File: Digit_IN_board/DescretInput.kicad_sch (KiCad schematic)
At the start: 21 parts, among them J4 DS1013-01-10RSiB-B (1), U5 HEF40106B (SO-14), U8 74LVC2G14

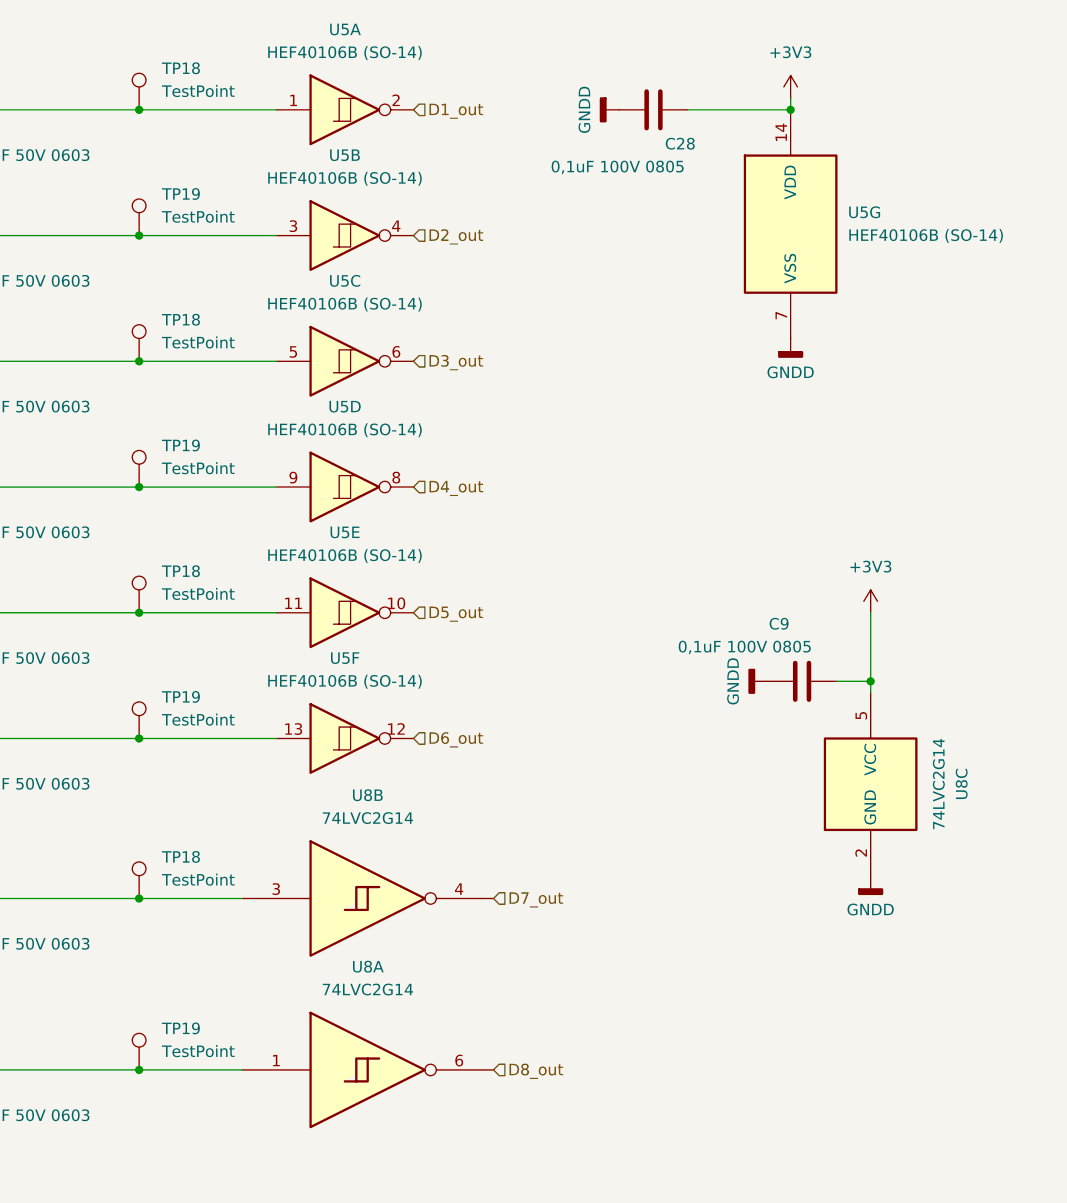
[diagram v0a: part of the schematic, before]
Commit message: Add DE USART 03.06.24
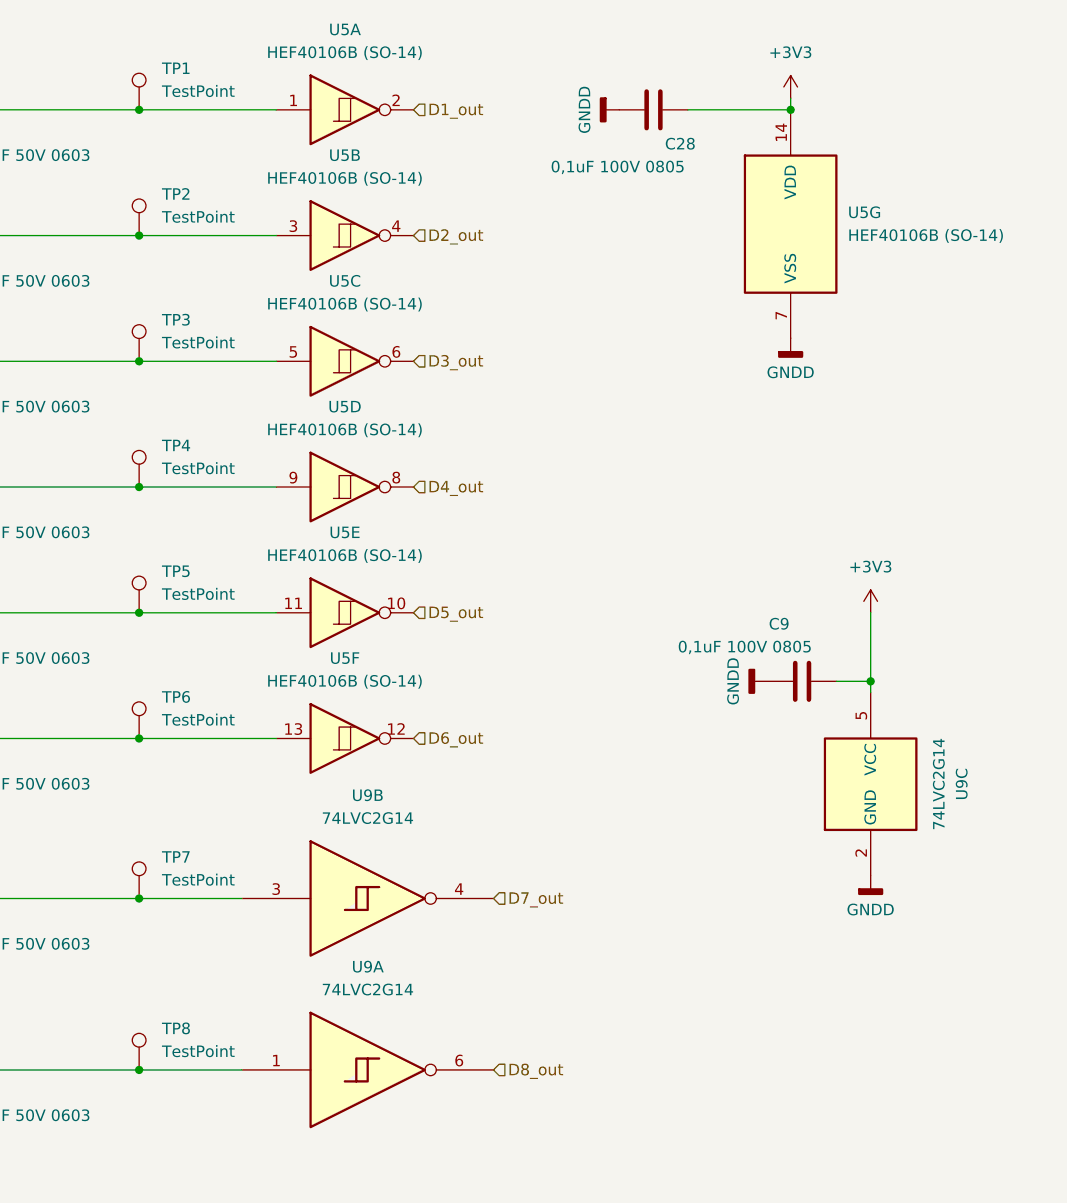
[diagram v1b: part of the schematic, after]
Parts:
- renumbered TP18 to TP1, TP19 to TP2, TP18 to TP3, TP19 to TP4, TP18 to TP5, TP19 to TP6, TP18 to TP7, TP19 to TP8, U8 to U9
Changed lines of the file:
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@@
   (symbol (lib_id "Connector:TestPoint") (at 185.42 100.33 0) (unit 1)
     (in_bom yes) (on_board yes) (dnp no) (fields_autoplaced)
-    (property "Reference" "TP19" (at 187.96 95.758 0)
+    (property "Reference" "TP6" (at 187.96 95.758 0)
       (effects (font (size 1.27 1.27)) (justify left))
     )
@@
   (symbol (lib_id "Connector:TestPoint") (at 185.42 58.42 0) (unit 1)
     (in_bom yes) (on_board yes) (dnp no)
-    (property "Reference" "TP18" (at 187.96 53.848 0)
+    (property "Reference" "TP3" (at 187.96 53.848 0)
       (effects (font (size 1.27 1.27)) (justify left))
     )
@@
   (symbol (lib_id "74xGxx:74LVC2G14") (at 266.7 105.41 0) (unit 3)
     (in_bom yes) (on_board yes) (dnp no) (fields_autoplaced)
-    (property "Reference" "U8" (at 276.86 105.41 90)
+    (property "Reference" "U9" (at 276.86 105.41 90)
       (effects (font (size 1.27 1.27)))
     )
@@
   (symbol (lib_id "Connector:TestPoint") (at 185.42 86.36 0) (unit 1)
     (in_bom yes) (on_board yes) (dnp no) (fields_autoplaced)
-    (property "Reference" "TP18" (at 187.96 81.788 0)
+    (property "Reference" "TP5" (at 187.96 81.788 0)
       (effects (font (size 1.27 1.27)) (justify left))
     )
@@
   (symbol (lib_id "74xGxx:74LVC2G14") (at 212.09 118.11 0) (unit 2)
     (in_bom yes) (on_board yes) (dnp no) (fields_autoplaced)
-    (property "Reference" "U8" (at 210.82 106.68 0)
+    (property "Reference" "U9" (at 210.82 106.68 0)
       (effects (font (size 1.27 1.27)))
     )
@@
   (symbol (lib_id "Connector:TestPoint") (at 185.42 30.48 0) (unit 1)
     (in_bom yes) (on_board yes) (dnp no) (fields_autoplaced)
-    (property "Reference" "TP18" (at 187.96 25.908 0)
+    (property "Reference" "TP1" (at 187.96 25.908 0)
       (effects (font (size 1.27 1.27)) (justify left))
     )
@@
   (symbol (lib_id "Connector:TestPoint") (at 185.42 118.11 0) (unit 1)
     (in_bom yes) (on_board yes) (dnp no) (fields_autoplaced)
-    (property "Reference" "TP18" (at 187.96 113.538 0)
+    (property "Reference" "TP7" (at 187.96 113.538 0)
       (effects (font (size 1.27 1.27)) (justify left))
     )
@@
   (symbol (lib_id "Connector:TestPoint") (at 185.42 44.45 0) (unit 1)
     (in_bom yes) (on_board yes) (dnp no) (fields_autoplaced)
-    (property "Reference" "TP19" (at 187.96 39.878 0)
+    (property "Reference" "TP2" (at 187.96 39.878 0)
       (effects (font (size 1.27 1.27)) (justify left))
     )
@@
   (symbol (lib_id "Connector:TestPoint") (at 185.42 137.16 0) (unit 1)
     (in_bom yes) (on_board yes) (dnp no) (fields_autoplaced)
-    (property "Reference" "TP19" (at 187.96 132.588 0)
+    (property "Reference" "TP8" (at 187.96 132.588 0)
       (effects (font (size 1.27 1.27)) (justify left))
     )
@@
   (symbol (lib_id "74xGxx:74LVC2G14") (at 212.09 137.16 0) (unit 1)
     (in_bom yes) (on_board yes) (dnp no) (fields_autoplaced)
-    (property "Reference" "U8" (at 210.82 125.73 0)
+    (property "Reference" "U9" (at 210.82 125.73 0)
       (effects (font (size 1.27 1.27)))
     )
@@
   (symbol (lib_id "Connector:TestPoint") (at 185.42 72.39 0) (unit 1)
     (in_bom yes) (on_board yes) (dnp no) (fields_autoplaced)
-    (property "Reference" "TP19" (at 187.96 67.818 0)
-      (effects (font (size 1.27 1.27)) (justify left))
-    )
+    (property "Reference" "TP4" (at 187.96 67.818 0)
+      (effects (font (size 1.27 1.27)) (justify left))
+    )

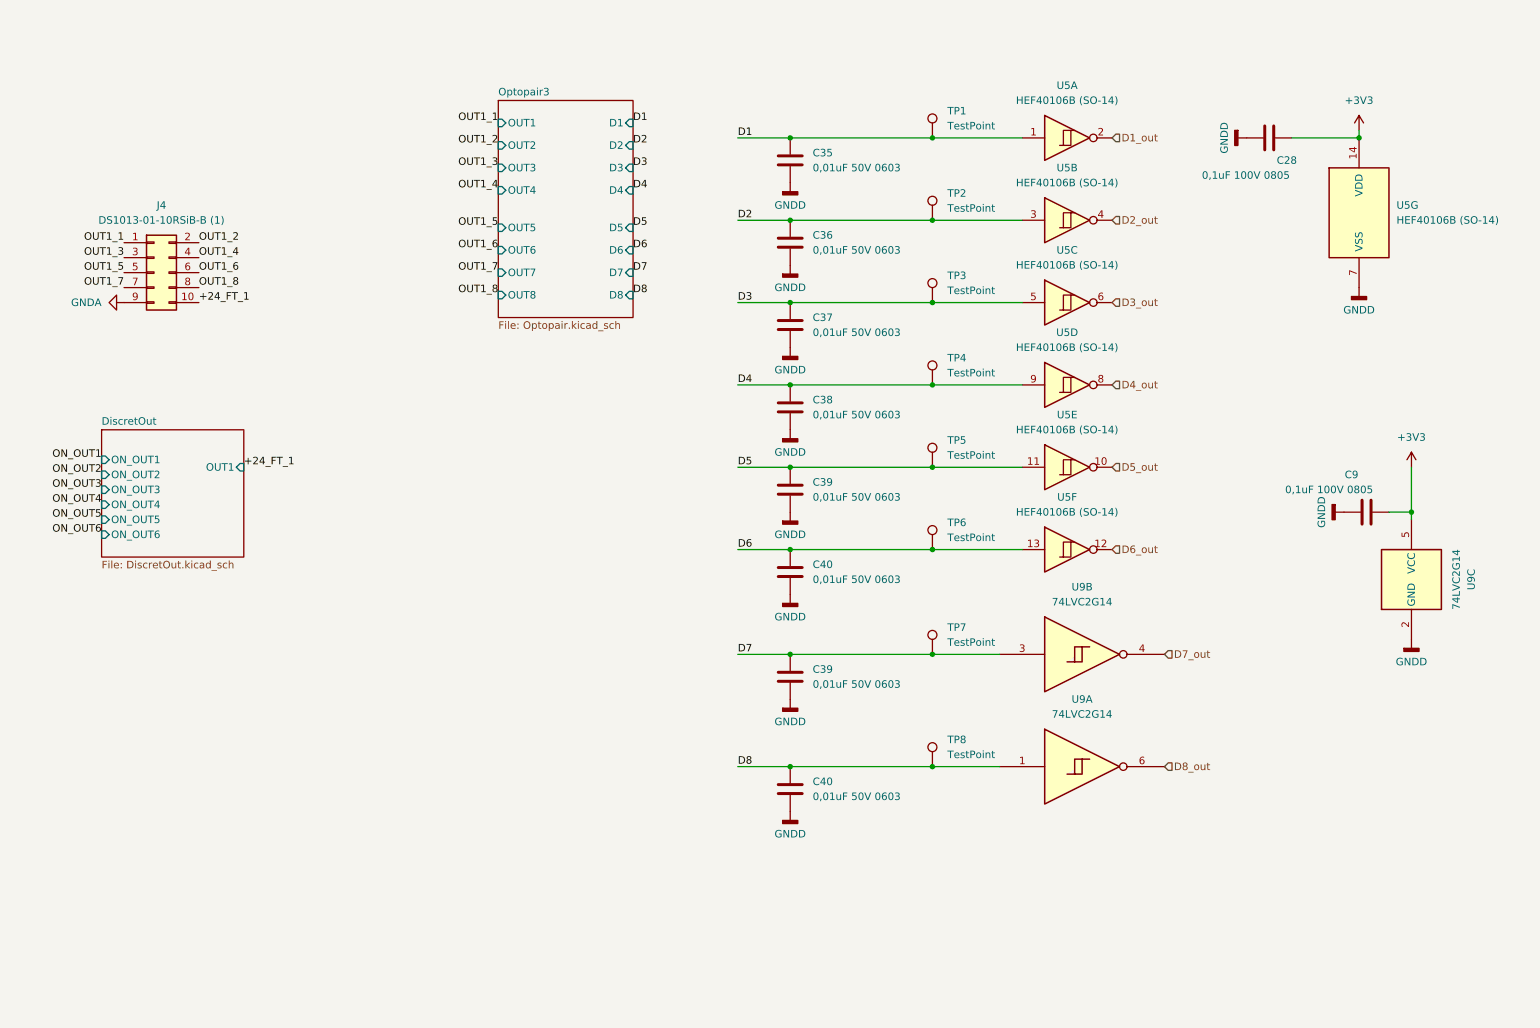
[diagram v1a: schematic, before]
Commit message: Discret IN OUT schems
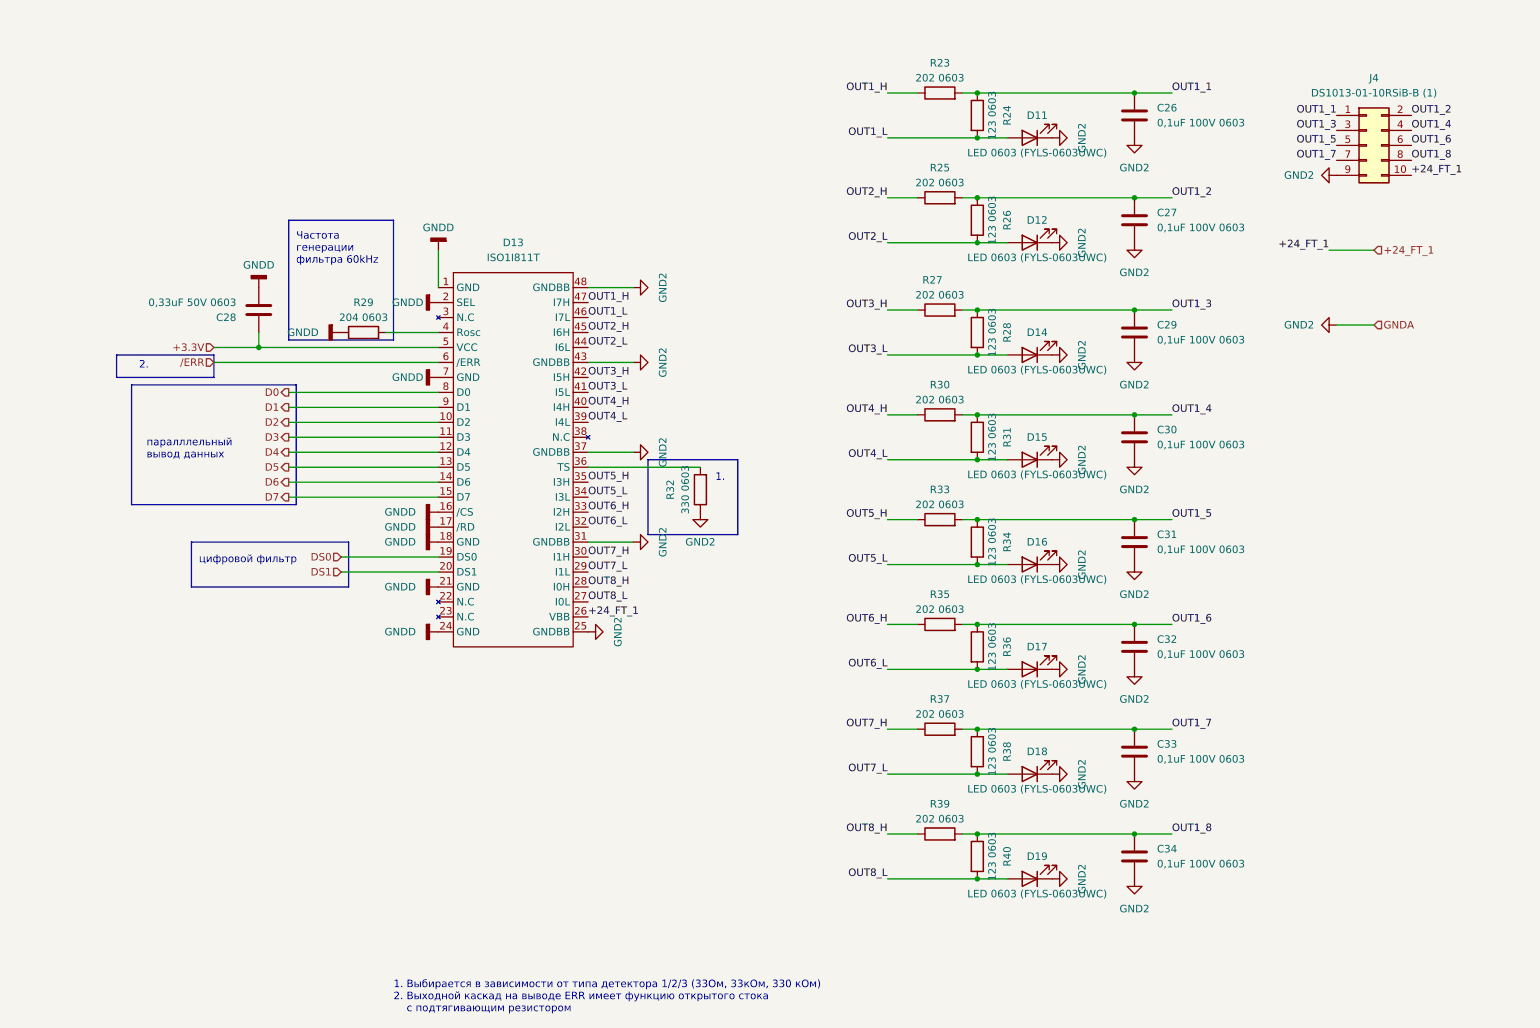
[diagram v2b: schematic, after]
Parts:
- removed C35, C36, C37, C38, C39 (x2), C40 (x2): 0,01uF 50V 0603, PCM_Capacitor_SMD_US_Handsoldering_AKL:C_0603_1608Metric_Pad1.08x0.95mm, symbol Device:C
- removed C9: 0,1uF 100V 0805, PCM_Capacitor_SMD_AKL:C_0805_2012Metric_Pad1.18x1.45mm_HandSolder, symbol Device:C
- removed TP1, TP2, TP3, TP4, TP5, TP6, TP7, TP8: TestPoint, PCM_4ms_TestPoint:TestPoint_D1, symbol Connector:TestPoint
- removed U5: HEF40106B (SO-14), Package_SO:SO-14_3.9x8.65mm_P1.27mm, symbol 4xxx:40106
- removed U9: 74LVC2G14, Package_TO_SOT_SMD:SOT-23-6, symbol 74xGxx:74LVC2G14
- added C26, C27, C29, C30, C31, C32, C33, C34: 0,1uF 100V 0603, Capacitor_SMD:C_0603_1608Metric_Pad1.08x0.95mm_HandSolder, symbol Device:C
- added D11, D12, D14, D15, D16, D17, D18, D19: LED 0603 (FYLS-0603UWC), LED_SMD:LED_0603_1608Metric_Pad1.05x0.95mm_HandSolder, symbol Device:LED
- added D13: ISO1I811T, Package_SO:TSSOP-48_6.1x12.5mm_P0.5mm, symbol Isolator:ISO1I811T
- added R23, R25, R27, R30, R33, R35, R37, R39: 202 0603, PCM_Resistor_SMD_AKL:R_0603_1608Metric_Pad1.05x0.95mm_HandSolder, symbol Device:R
- added R24, R26, R28, R31, R34, R36, R38, R40: 123 0603, PCM_Resistor_SMD_AKL:R_0603_1608Metric_Pad1.05x0.95mm_HandSolder, symbol Device:R
- added R29: 204 0603, Capacitor_SMD:C_0603_1608Metric_Pad1.08x0.95mm_HandSolder, symbol Device:R
- added R32: 330 0603, PCM_Resistor_SMD_AKL:R_0603_1608Metric_Pad1.05x0.95mm_HandSolder, symbol Device:R
- C28: value 0,1uF 100V 0805 -> 0,33uF 50V 0603; footprint PCM_Resistor_SMD_AKL:R_0805_2012Metric_Pad1.20x1.40mm_HandSolder -> Capacitor_SMD:C_0603_1608Metric_Pad1.08x0.95mm_HandSolder
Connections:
- net +24_FT_1: now also D13.26 (VBB)
- net D1: now also D13.9 (D1)
- net D2: now also D13.10 (D2)
- net D3: now also D13.11 (D3)
- net D4: now also D13.12 (D4)
- net D5: now also D13.13 (D5)
- net D6: now also D13.14 (D6)
- net D7: now also D13.15 (D7)
- net GNDD: now also D13.1 (GND), D13.16 (/CS), D13.17 (/RD), D13.18 (GND), D13.2 (SEL), D13.21 (GND), D13.24 (GND), D13.7 (GND), R29.1
- net OUT1_1: now also C26.1, R23.2, R24.1
- net OUT1_2: now also C27.1, R25.2, R26.1
- net OUT1_3: now also C29.1, R27.2, R28.1
- net OUT1_4: now also C30.1, R30.2, R31.1
- net OUT1_5: now also C31.1, R33.2, R34.1
- net OUT1_6: now also C32.1, R35.2, R36.1
- net OUT1_7: now also C33.1, R37.2, R38.1
- net OUT1_8: now also C34.1, R39.2, R40.1
- net +3V3 renamed +3.3V
- net +3.3V: now also D13.5 (VCC)
- net GNDA renamed GND2
- net GND2: now also C26.2, C27.2, C29.2, C30.2, C31.2, C32.2, C33.2, C34.2, D11.1 (K), D12.1 (K), D13.25 (GNDBB), D13.31 (GNDBB), D13.37 (GNDBB), D13.43 (GNDBB), D13.48 (GNDBB), D14.1 (K), D15.1 (K), D16.1 (K), D17.1 (K), D18.1 (K), D19.1 (K), R32.1
- new net: D13.4 (Rosc), R29.2
- new net: D13.36 (TS), R32.2
- new net D0: D13.8 (D0)
- new net DS0: D13.19 (DS0)
- new net DS1: D13.20 (DS1)
- new net OUT1_H: D13.47 (I7H), R23.1
- new net OUT1_L: D11.2 (A), D13.46 (I7L), R24.2
- new net OUT2_H: D13.45 (I6H), R25.1
- new net OUT2_L: D12.2 (A), D13.44 (I6L), R26.2
- new net OUT3_H: D13.42 (I5H), R27.1
- new net OUT3_L: D13.41 (I5L), D14.2 (A), R28.2
- new net OUT4_H: D13.40 (I4H), R30.1
- new net OUT4_L: D13.39 (I4L), D15.2 (A), R31.2
- new net OUT5_H: D13.35 (I3H), R33.1
- new net OUT5_L: D13.34 (I3L), D16.2 (A), R34.2
- new net OUT6_H: D13.33 (I2H), R35.1
- new net OUT6_L: D13.32 (I2L), D17.2 (A), R36.2
- new net OUT7_H: D13.30 (I1H), R37.1
- new net OUT7_L: D13.29 (I1L), D18.2 (A), R38.2
- new net OUT8_H: D13.28 (I0H), R39.1
- new net OUT8_L: D13.27 (I0L), D19.2 (A), R40.2
- new net /ERR: D13.6 (/ERR)
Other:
- removed sheet DiscretOut
- removed sheet Optopair3
- note added: "1."
- note added: "1. Выбирается в зависимости от типа детектора 1/2/3 (33Ом, 33кОм, 330 кОм) 2. Выходной каскад на выводе ERR имеет функцию открытого стока с подтягивающим резистором"
- note added: "2."
- note added: "Частота генерации фильтра 60kHz"
- note added: "паралллельный вывод данных"
- note added: "цифровой фильтр"
- moved on the sheet: J4
